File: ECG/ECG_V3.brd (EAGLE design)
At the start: 69.8 x 39.4 mm, 32 parts, among them U1 AD8232, U3 BGM111-VISUAL-A

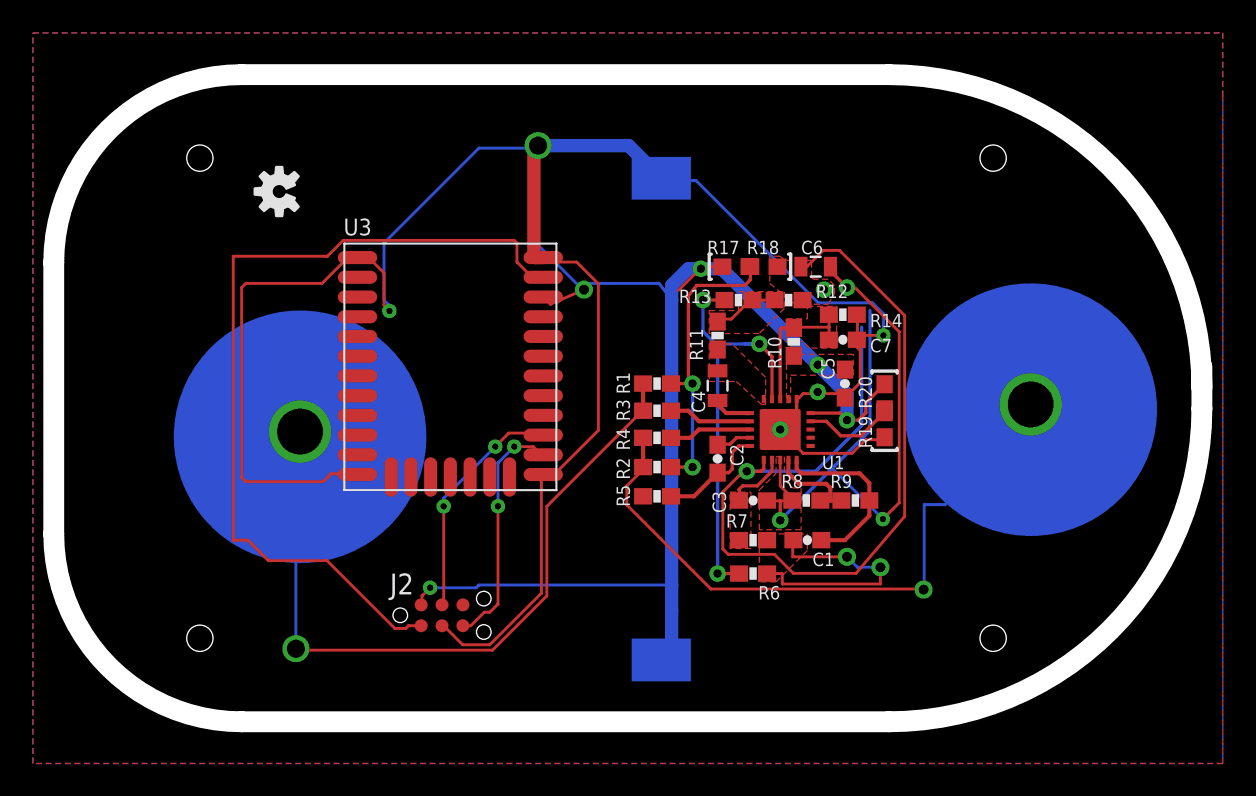
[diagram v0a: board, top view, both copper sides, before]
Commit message: Corrected thepolygon issues, thickened connections to pad and resolved clearance issues
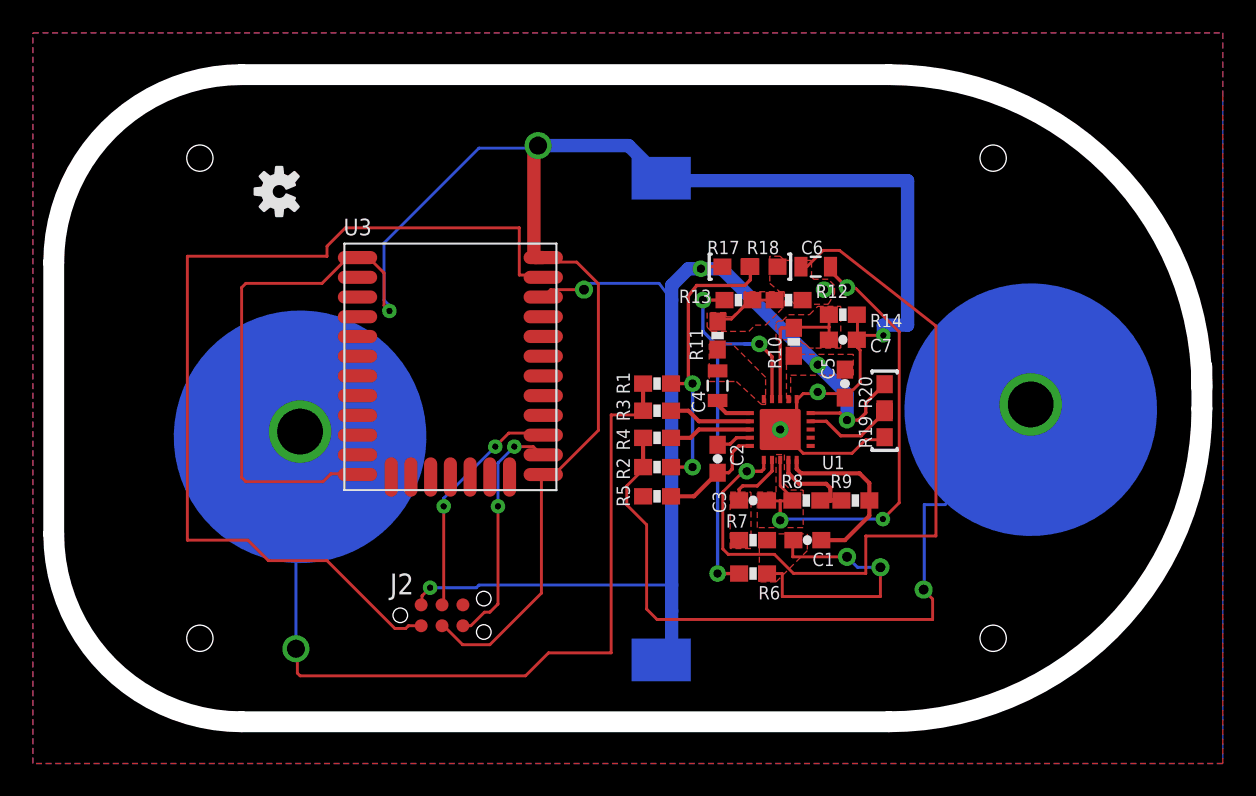
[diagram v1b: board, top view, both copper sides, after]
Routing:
- net REFOUT: track 42.9 -> 29.8 mm
- net N$16: track 55.1 -> 46.0 mm
- net N$29: track 51.9 -> 60.3 mm
- net GND: track 134.9 -> 142.6 mm
- net LA: track 45.3 -> 53.0 mm
- net RA: track 39.2 -> 45.7 mm
- net 3.3V: track 79.5 -> 73.2 mm
- net N$9: track 15.2 -> 16.7 mm
